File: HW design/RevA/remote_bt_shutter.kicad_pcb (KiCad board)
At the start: 2 copper layers, 50.2 x 73.2 mm, 48 parts, among them K1 NIKON_CONN, P1 ICSP, P10 PWR_SW, P3 MODE_SW, P4 SW1, P5 TP_BT_RX, P6 TP_BT_TX, P7 SW2, P8 SW3, P9 BATT_CONN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

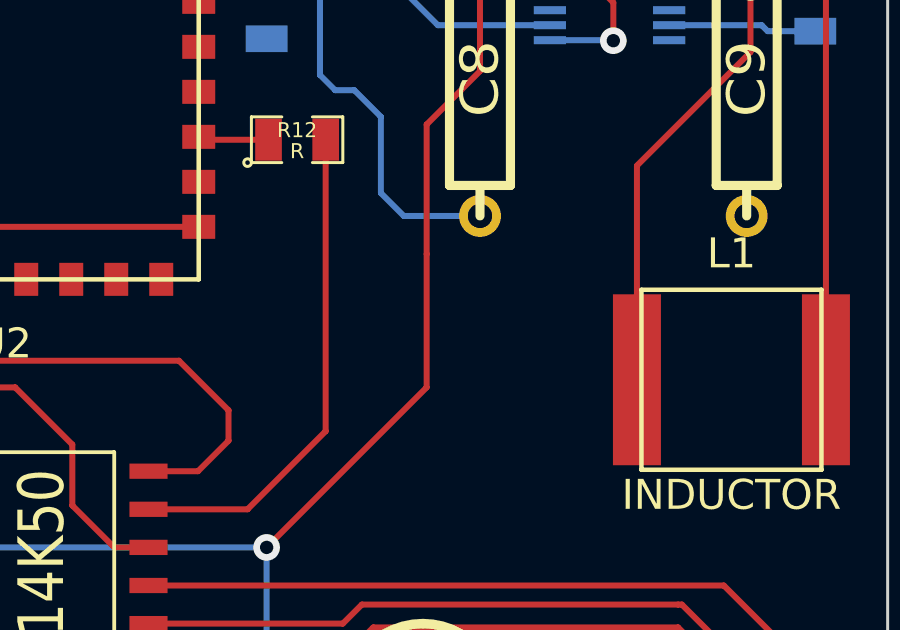
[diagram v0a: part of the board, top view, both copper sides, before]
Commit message: Added a diode from power circuit
To be on the safe side, added a diode to protect the power circuit from any current from the ICSP prommer. Is actually a shorted connector which can be in time of catastrophy have the trace cut and diode added.
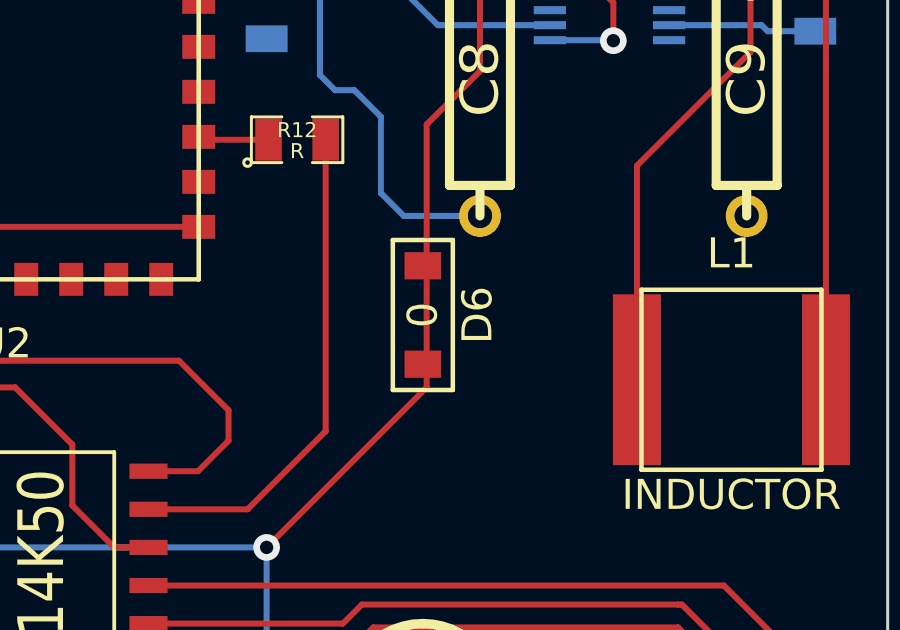
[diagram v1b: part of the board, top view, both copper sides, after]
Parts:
- added D6: 0, SOD-123, F.Cu at (214.6, 162.4)

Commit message: PCB layout almost done
PCB layout done otherwise except for front ground
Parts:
- D1, D2, R11, R7, R8, R9: moved to B.Cu
- moved C1 82.6 mm to (221.6, 170.1), turned to 180 degrees
- moved R1 77.5 mm to (218.8, 166.9), turned to 270 degrees
- moved R9 62.8 mm to (198.9, 157.2), turned to 90 degrees
- moved D1 57.6 mm to (217.0, 173.1), turned to 180 degrees
- moved P4 55.0 mm to (187.3, 183.9), turned to 180 degrees
- moved D2 54.3 mm to (217.0, 170.1), turned to 180 degrees
- moved P7 51.5 mm to (185.2, 177.7), turned to 90 degrees
- moved R7 49.1 mm to (188.8, 176.3), turned to 90 degrees
- moved R11 47.2 mm to (193.2, 169.2), turned to 90 degrees
- moved D3 45.9 mm to (186.8, 151.4), turned to 270 degrees
- moved R8 44.1 mm to (191.1, 174.2), turned to 90 degrees
- moved R6 43.6 mm to (191.0, 176.3), turned to 90 degrees
- moved P8 43.1 mm to (185.9, 162.3), turned to 270 degrees
- moved P3 39.6 mm to (186.6, 171.1)
- moved R13 0.38 mm to (213.7, 146.6)
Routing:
- net /LOW_BATT_IND: track 0.00 -> 50.6 mm
- net +3.3V: track 91.4 -> 133.6 mm, vias 3 -> 5
- net N-000001: track 21.0 -> 48.2 mm, vias 1 -> 2
- net N-0000015: track 4.95 -> 26.0 mm, vias 0 -> 4
- net N-000008: track 0.00 -> 17.7 mm
- net N-000004: track 0.00 -> 16.1 mm
- net N-000009: track 0.00 -> 16.0 mm
- net N-0000011: track 0.00 -> 15.9 mm
- net N-0000010: track 0.00 -> 15.8 mm, vias 0 -> 1
- net GND: track 79.5 -> 93.3 mm
- net N-000007: track 0.00 -> 13.9 mm, vias 0 -> 1
- net N-0000021: track 0.00 -> 13.4 mm, vias 0 -> 1
- net N-0000022: track 0.00 -> 9.91 mm, vias 0 -> 1
- net N-000002: track 0.00 -> 7.19 mm, vias 0 -> 1
- net N-0000020: track 0.00 -> 2.76 mm
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
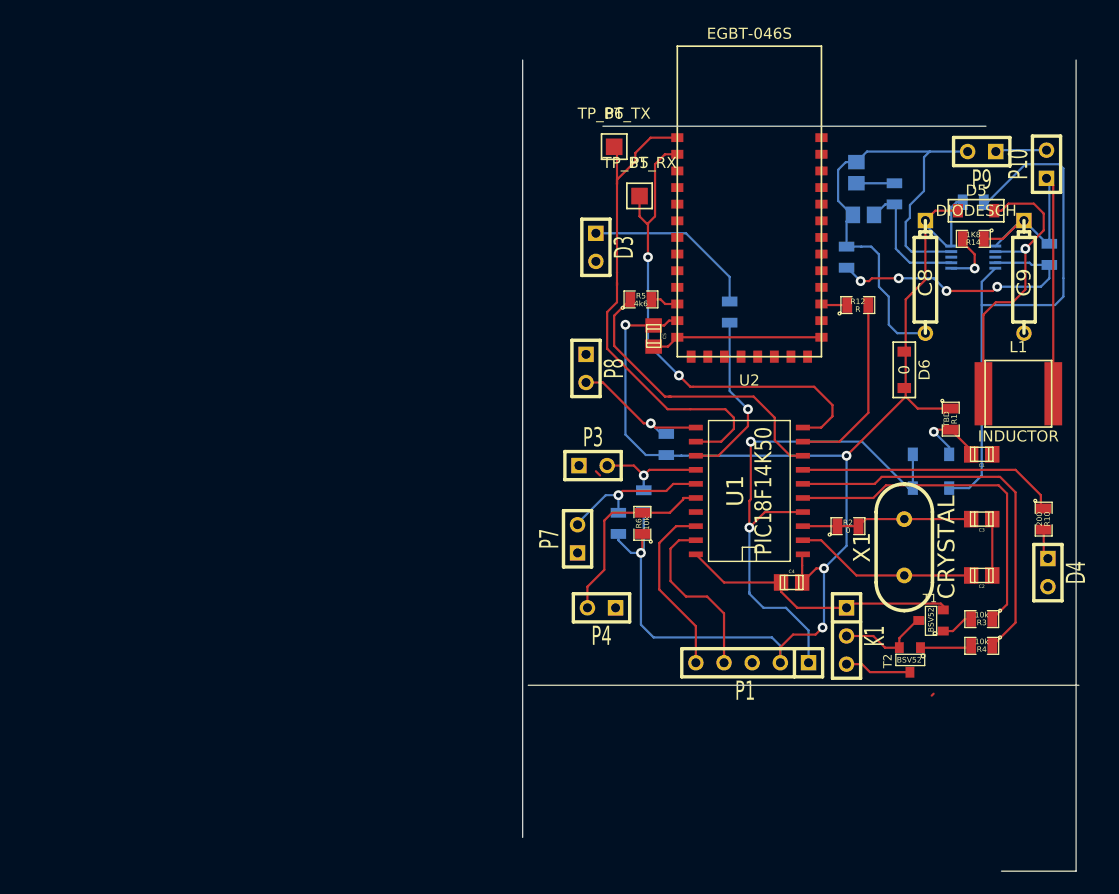
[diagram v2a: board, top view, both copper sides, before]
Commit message: PCB layout finished
Layout finished, still need to add board edges
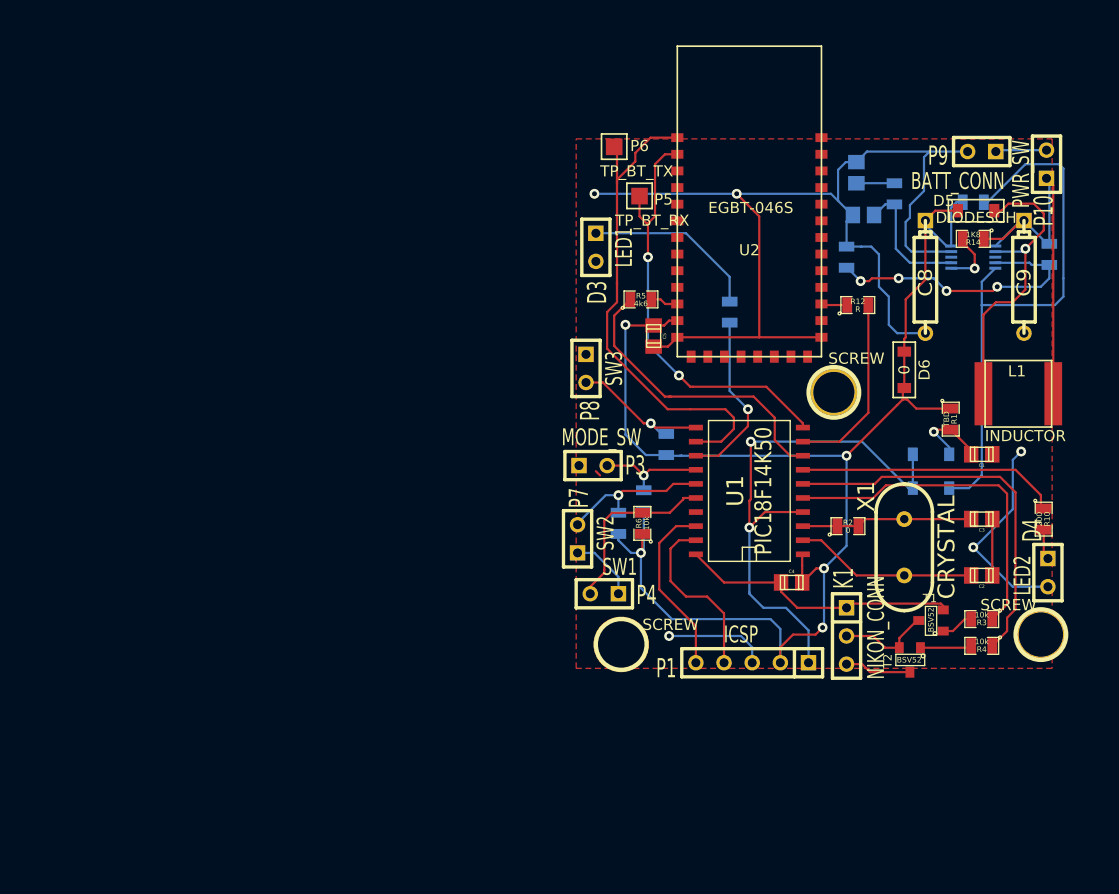
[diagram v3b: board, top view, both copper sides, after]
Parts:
- added SCREW: P***, 1pin, F.Cu at (208.3, 164.5)
- added SCREW: P***, 1pin, F.Cu at (189.1, 187.2)
- added SCREW: P***, 1pin, F.Cu at (226.9, 186.3)
- D3: value LED -> LED1
- D4: value LED -> LED2
- moved P4 1.30 mm to (187.6, 182.6)
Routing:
- net GND: track 93.3 -> 163.5 mm, vias 0 -> 5
- net N-0000038: track 44.8 -> 39.1 mm
- net N-000008: track 17.7 -> 16.3 mm
- net +3.3V: track 133.6 -> 132.8 mm
- added copper zone on F.Cu, net GND
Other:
- board outline removed

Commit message: PCB layout final
PCB layout finished, ready for printing.
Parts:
- moved T2 0.40 mm to (215.3, 188.2)
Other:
- board outline added: 46.1 x 49.7 mm
- board text added: "1.5V->3.3V booster"
- board text added: "Bluetooth-remote This device is a Bluetooth remote controller. It has a possibility to trigger Nikon SLD over BT (Android app), or to use as a general purpose Bluetooth remote. Such as with a table hockey app. Karri Kivelä 06/2015 karrister@gmail.com www.karrikivela.fi"
- board text added: "Bluetooth-remote www.karrikivela.fi karrister@gmail.com"
- board text added: "KORSO"
- board text added: "Karri Kivelä 6/2015 www.karrikivela.fi"
- board text added: "Korso"
- board text added: "www.karrikivela.fi"
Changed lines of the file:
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@@
     (links 94)
     (no_connects 0)
-    (area 180.162999 131.286 231.39527 207.695001)
+    (area 182.992889 132.915999 231.281153 191.699444)
     (thickness 1.6)
-    (drawings 0)
-    (tracks 390)
+    (drawings 13)
+    (tracks 395)
     (zones 0)
     (modules 52)
@@
   )
   (module SOT23 (layer F.Cu)
-    (at 215.138 188.595 180)
+    (at 215.265 188.214 180)
     (tags SOT23)
     (fp_text reference T2 (at 1.99898 -0.09906 270) (layer F.SilkS)
@@
   (module EGBT-046S (layer F.Cu)
     (at 200.66 150.495)
-    (fp_text reference U2 (at 0 1.143) (layer F.SilkS)
+    (fp_text reference U2 (at 0 -0.889) (layer F.SilkS)
       (effects (font (size 1 1) (thickness 0.15)))
     )
@@
     )
   )
+  (gr_text Korso (at 200.533 159.004) (layer F.SilkS)
+    (effects (font (size 1.5 1.5) (thickness 0.3)))
+  )
+  (gr_text KORSO (at 200.66 153.162) (layer F.SilkS)
+    (effects (font (size 1.5 1.5) (thickness 0.3)))
+  )
+  (gr_text Korso (at 200.533 144.018) (layer F.SilkS)
+    (effects (font (size 1.5 1.5) (thickness 0.3)))
+  )
+  (gr_text www.karrikivela.fi (at 222.377 189.484) (layer B.SilkS)
+    (effects (font (size 0.9 0.9) (thickness 0.225)) (justify mirror))
+  )
+  (gr_text www.karrikivela.fi (at 222.377 189.357) (layer F.SilkS)
+    (effects (font (size 0.9 0.9) (thickness 0.225)))
+  )
+  (gr_text "1.5V->3.3V\nbooster" (at 213.106 148.082 90) (layer F.SilkS)
+    (effects (font (size 1 1) (thickness 0.2)))
+  )
+  (gr_text "Bluetooth-remote\nThis device is a Bluetooth remote controller.\nIt has a possibility to trigger Nikon SLD\nover BT (Android app), or to use as a\ngeneral              purpose Bluetooth\nremote.             Such as with a table\nhockey              app.\n\nKarri Kivelä 06/2015\nkarrister@gmail.com\nwww.karrikivela.fi" (at 205.486 156.464) (layer B.SilkS)
+    (effects (font (size 1 1) (thickness 0.25)) (justify mirror))
+  )
+  (gr_text "Karri Kivelä 6/2015\nwww.karrikivela.fi" (at 198.501 180.594) (layer F.SilkS)
+    (effects (font (size 0.9 0.9) (thickness 0.2)))
+  )
+  (gr_text "Bluetooth-remote\nwww.karrikivela.fi\nkarrister@gmail.com" (at 198.755 163.068) (layer F.SilkS)
+    (effects (font (size 0.8 0.8) (thickness 0.2)))
+  )
+  (gr_line (start 229.6 140.7) (end 183.5 140.7) (angle 90) (layer Edge.Cuts) (width 0.1))
+  (gr_line (start 229.6 190.4) (end 229.6 140.7) (angle 90) (layer Edge.Cuts) (width 0.1))
+  (gr_line (start 183.5 190.4) (end 229.6 190.4) (angle 90) (layer Edge.Cuts) (width 0.1))
+  (gr_line (start 183.5 140.7) (end 183.5 190.4) (angle 90) (layer Edge.Cuts) (width 0.1))
   (segment (start 187.198 171.958) (end 186.817 171.577) (width 0.2) (layer F.Cu) (net 0))
   (segment (start 203.454 187.325) (end 203.454 185.801) (width 0.2) (layer B.Cu) (net 1))
@@
   (segment (start 205.486 171.45) (end 224.663 171.45) (width 0.2) (layer F.Cu) (net 11))
   (segment (start 226.949 174.6885) (end 227.203 174.9425) (width 0.2) (layer F.Cu) (net 11))
-  (segment (start 209.423 188.976) (end 210.82 188.976) (width 0.2) (layer F.Cu) (net 12))
-  (segment (start 211.53882 189.69482) (end 215.138 189.69482) (width 0.2) (layer F.Cu) (net 12))
-  (segment (start 210.82 188.976) (end 211.53882 189.69482) (width 0.2) (layer F.Cu) (net 12))
+  (segment (start 215.265 189.31382) (end 213.57082 189.31382) (width 0.2) (layer F.Cu) (net 12))
+  (segment (start 210.82 188.976) (end 209.423 188.976) (width 0.2) (layer F.Cu) (net 12))
+  (segment (start 213.233 188.976) (end 210.82 188.976) (width 0.2) (layer F.Cu) (net 12))
+  (segment (start 213.57082 189.31382) (end 213.233 188.976) (width 0.2) (layer F.Cu) (net 12))
   (segment (start 214.122 151.765) (end 213.868 151.511) (width 0.2) (layer B.Cu) (net 13))
   (segment (start 214.122 151.765) (end 215.13 152.773) (width 0.2) (layer B.Cu) (net 13))
@@
   (segment (start 191.135 171.958) (end 191.643 171.45) (width 0.2) (layer F.Cu) (net 17))
   (via (at 191.135 171.958) (size 0.889) (layers F.Cu B.Cu) (net 17))
-  (segment (start 216.0905 187.49518) (end 220.49232 187.49518) (width 0.2) (layer F.Cu) (net 18))
-  (segment (start 220.49232 187.49518) (end 220.6625 187.325) (width 0.2) (layer F.Cu) (net 18))
+  (segment (start 220.6625 187.325) (end 216.42832 187.325) (width 0.2) (layer F.Cu) (net 18))
+  (segment (start 216.42832 187.325) (end 216.2175 187.11418) (width 0.2) (layer F.Cu) (net 18))
   (segment (start 223.139 172.847) (end 223.901 173.609) (width 0.2) (layer F.Cu) (net 19))
   (segment (start 223.139 172.847) (end 212.979 172.847) (width 0.2) (layer F.Cu) (net 19))
@@
   (segment (start 210.312 180.975) (end 214.63 180.975) (width 0.2) (layer F.Cu) (net 22))
   (segment (start 207.137 177.8) (end 210.312 180.975) (width 0.2) (layer F.Cu) (net 22))
-  (segment (start 214.1855 187.49518) (end 212.89518 187.49518) (width 0.2) (layer F.Cu) (net 23))
+  (segment (start 214.3125 187.11418) (end 213.82482 187.11418) (width 0.2) (layer F.Cu) (net 23))
+  (segment (start 213.487 187.452) (end 212.852 187.452) (width 0.2) (layer F.Cu) (net 23))
+  (segment (start 213.82482 187.11418) (end 213.487 187.452) (width 0.2) (layer F.Cu) (net 23))
+  (segment (start 214.3125 187.11418) (end 214.3125 186.8805) (width 0.2) (layer F.Cu) (net 23))
+  (segment (start 215.94318 185.24982) (end 215.94318 185.039) (width 0.2) (layer F.Cu) (net 23))
+  (segment (start 214.3125 186.8805) (end 215.94318 185.24982) (width 0.2) (layer F.Cu) (net 23))
+  (segment (start 212.89518 187.49518) (end 212.852 187.452) (width 0.2) (layer F.Cu) (net 23))
+  (segment (start 212.852 187.452) (end 211.836 186.436) (width 0.2) (layer F.Cu) (net 23))
   (segment (start 211.836 186.436) (end 209.423 186.436) (width 0.2) (layer F.Cu) (net 23))
-  (segment (start 212.89518 187.49518) (end 211.836 186.436) (width 0.2) (layer F.Cu) (net 23))
   (segment (start 215.94318 185.039) (end 215.773 185.039) (width 0.2) (layer F.Cu) (net 23))
-  (segment (start 214.1855 186.6265) (end 214.1855 187.49518) (width 0.2) (layer F.Cu) (net 23))
-  (segment (start 215.773 185.039) (end 214.1855 186.6265) (width 0.2) (layer F.Cu) (net 23))
   (segment (start 220.6625 184.912) (end 220.091 184.912) (width 0.2) (layer F.Cu) (net 24))
   (segment (start 219.0115 185.9915) (end 218.14282 185.9915) (width 0.2) (layer F.Cu) (net 24))
